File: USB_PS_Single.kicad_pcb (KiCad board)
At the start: 2 copper layers, 24.5 x 24.4 mm, 12 parts, among them P1 CONN_02X08, P2 CONN_01X06, P3 USB_B, P4 CONN_01X01, P5 CONN_01X01

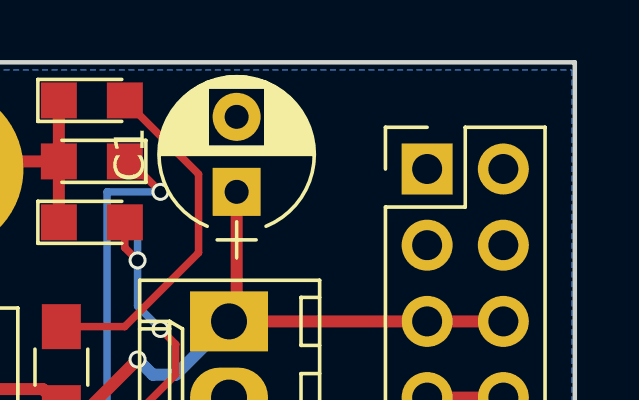
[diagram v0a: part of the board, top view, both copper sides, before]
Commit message: Updated labels
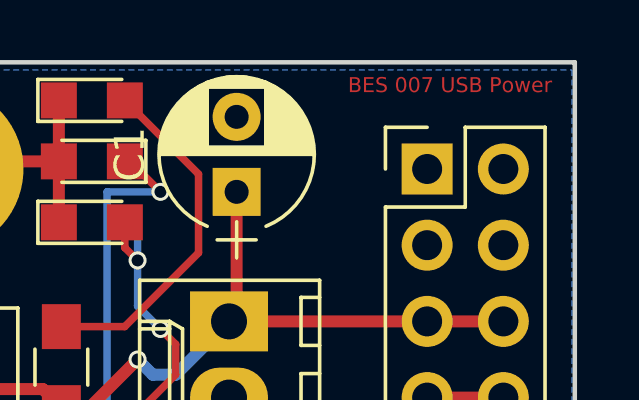
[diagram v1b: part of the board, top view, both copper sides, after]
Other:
- board text added: "BES 007 USB Power"
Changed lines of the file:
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@@
     (links 29)
     (no_connects 0)
-    (area 58.598999 42.594999 83.229001 67.131001)
+    (area 43.480667 41.453 84.535334 68.375)
     (thickness 1.6)
-    (drawings 7)
+    (drawings 8)
     (tracks 68)
     (zones 0)
@@
   (layers
     (0 F.Cu signal)
-    (31 B.Cu signal)
+    (31 B.Cu signal hide)
     (32 B.Adhes user)
     (33 F.Adhes user)
@@
     (pad_to_mask_clearance 0.2)
     (aux_axis_origin 0 0)
-    (visible_elements FFFFFF7F)
+    (visible_elements 7FFFFF7F)
     (pcbplotparams
       (layerselection 0x00030_80000001)
@@
       (net 2 GND))
   )
+  (gr_text "BES 007 USB Power" (at 78.994 43.434) (layer F.Cu)
+    (effects (font (size 0.5 0.5) (thickness 0.125)))
+  )
   (gr_text "Barry Synnott\nBox Emissions Systems" (at 67.056 55.372 90) (layer B.SilkS)
     (effects (font (size 0.5 0.5) (thickness 0.125)) (justify mirror))
@@
   (gr_line (start 83.154 42.67) (end 83.154 67.05) (angle 90) (layer Edge.Cuts) (width 0.15))
   (gr_line (start 58.674 42.672) (end 83.154 42.672) (angle 90) (layer Edge.Cuts) (width 0.15))
-  (segment (start 66.04 54.182) (end 66.976 54.182) (width 0.4) (layer F.Cu) (net 1) (status 400000))
-  (segment (start 69.85 53.086) (end 71.628 51.308) (width 0.4) (layer B.Cu) (net 1) (status 800000))
+  (segment (start 66.04 54.182) (end 66.976 54.182) (width 0.4) (layer F.Cu) (net 1))
+  (segment (start 69.85 53.086) (end 71.628 51.308) (width 0.4) (layer B.Cu) (net 1))
   (segment (start 69.088 53.086) (end 69.85 53.086) (width 0.4) (layer B.Cu) (net 1))
   (segment (start 68.58 52.578) (end 69.088 53.086) (width 0.4) (layer B.Cu) (net 1))
   (via (at 68.58 52.578) (size 0.6) (drill 0.4) (layers F.Cu B.Cu) (net 1))
   (segment (start 66.976 54.182) (end 68.58 52.578) (width 0.4) (layer F.Cu) (net 1))
-  (segment (start 62.968 53.564) (end 65.422 53.564) (width 0.4) (layer F.Cu) (net 1) (status C00000))
-  (segment (start 65.422 53.564) (end 66.04 54.182) (width 0.4) (layer F.Cu) (net 1) (status C00000))
+  (segment (start 62.968 53.564) (end 65.422 53.564) (width 0.4) (layer F.Cu) (net 1))
+  (segment (start 65.422 53.564) (end 66.04 54.182) (width 0.4) (layer F.Cu) (net 1))
   (segment (start 71.374 46.99) (end 71.882 46.99) (width 0.4) (layer B.Cu) (net 1))
   (segment (start 71.628 51.308) (end 78.232 51.308) (width 0.4) (layer F.Cu) (net 1))
@@
   (segment (start 71.628 51.308) (end 71.882 51.054) (width 0.4) (layer F.Cu) (net 1))
   (segment (start 71.882 51.054) (end 71.882 46.99) (width 0.4) (layer F.Cu) (net 1))
-  (segment (start 62.968 56.164) (end 61.946 56.164) (width 0.4) (layer F.Cu) (net 2) (status 400000))
-  (segment (start 61.722 56.388) (end 61.722 63.246) (width 0.4) (layer F.Cu) (net 2) (status 800000))
+  (segment (start 62.968 56.164) (end 61.946 56.164) (width 0.4) (layer F.Cu) (net 2))
+  (segment (start 61.722 56.388) (end 61.722 63.246) (width 0.4) (layer F.Cu) (net 2))
   (segment (start 61.946 56.164) (end 61.722 56.388) (width 0.4) (layer F.Cu) (net 2))
-  (segment (start 61.722 63.246) (end 61.976 63.5) (width 0.4) (layer F.Cu) (net 2) (status C00000))
-  (segment (start 62.968 56.164) (end 62.968 55.514) (width 0.4) (layer F.Cu) (net 2) (status C00000))
+  (segment (start 61.722 63.246) (end 61.976 63.5) (width 0.4) (layer F.Cu) (net 2))
+  (segment (start 62.968 56.164) (end 62.968 55.514) (width 0.4) (layer F.Cu) (net 2))
   (segment (start 65.956 45.974) (end 62.23 45.974) (width 0.4) (layer F.Cu) (net 2))
   (segment (start 62.23 45.974) (end 61.976 46.228) (width 0.4) (layer F.Cu) (net 2))
